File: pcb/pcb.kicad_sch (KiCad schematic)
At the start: 71 parts, among them J1 WH, J2 RGB, J3 220, Q1 AO3400A, Q2 AO3400A, Q3 AO3400A, Q4 AO3400A, Q5 AOD452, Q6 DTD114E, Q7 AO3400A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

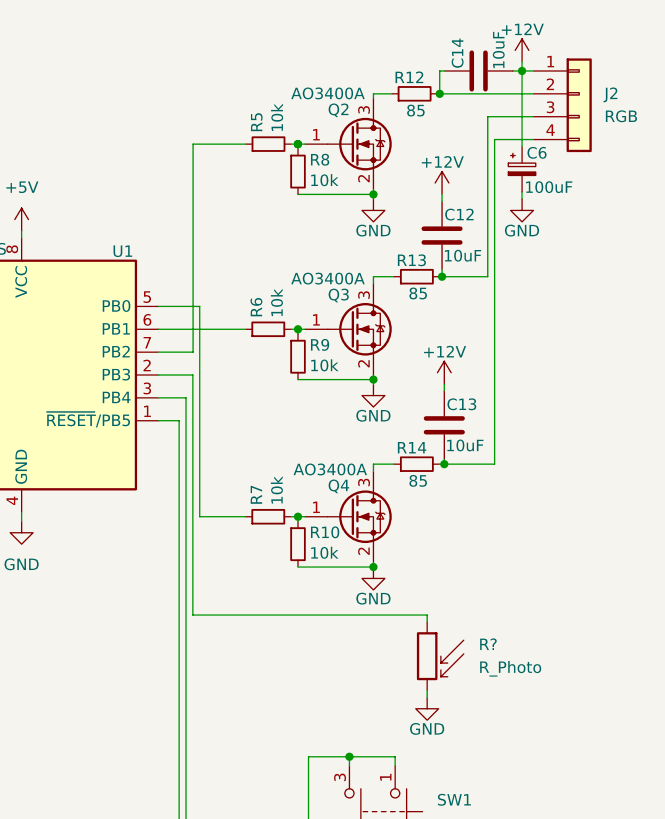
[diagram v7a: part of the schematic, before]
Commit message: light sensor added completely
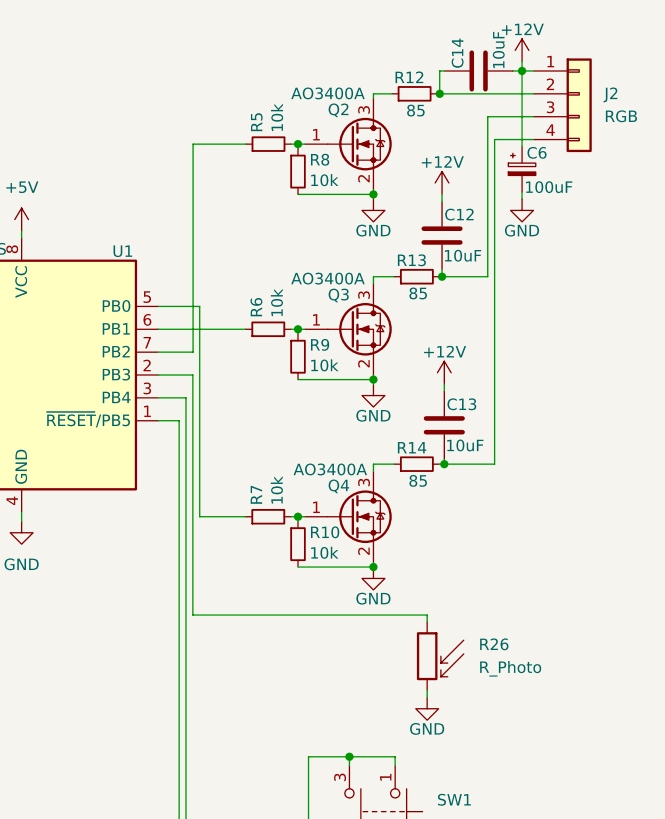
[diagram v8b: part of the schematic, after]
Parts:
- R26: renamed from R?; footprint (none) -> LED_THT:LED_D3.0mm
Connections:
- net at Q2.1 (G), R8.1: now also R5.2
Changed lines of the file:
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@@
   (junction (at 132.7404 45.974) (diameter 0) (color 0 0 0 0)
   )
+  (junction (at 230.759 27.432) (diameter 0) (color 0 0 0 0)
+  )
   (junction (at 76.3524 65.786) (diameter 0) (color 0 0 0 0)
   )
@@
   (junction (at 230.759 48.006) (diameter 0) (color 0 0 0 0)
   )
-  (junction (at 230.759 27.432) (diameter 0) (color 0 0 0 0)
-  )
   (junction (at 126.2634 65.786) (diameter 0) (color 0 0 0 0)
   )
@@
   (junction (at 173.8884 65.786) (diameter 0) (color 0 0 0 0)
   )
-  (junction (at 230.7336 27.432) (diameter 0) (color 0 0 0 0)
-  )
   (junction (at 118.7704 30.48) (diameter 0) (color 0 0 0 0)
   )
@@
     (stroke (width 0) (type default) (color 0 0 0 0))
   )
-  (wire (pts (xy 230.759 27.94) (xy 230.759 27.432))
-    (stroke (width 0) (type default) (color 0 0 0 0))
-  )
   (wire (pts (xy 132.7404 52.07) (xy 132.7404 53.848))
     (stroke (width 0) (type default) (color 0 0 0 0))
@@
     (stroke (width 0) (type default) (color 0 0 0 0))
   )
+  (wire (pts (xy 230.759 27.432) (xy 230.759 27.94))
+    (stroke (width 0) (type default) (color 0 0 0 0))
+  )
   (wire (pts (xy 247.015 62.992) (xy 252.603 62.992))
     (stroke (width 0) (type default) (color 0 0 0 0))
@@
     (stroke (width 0) (type default) (color 0 0 0 0))
   )
+  (wire (pts (xy 219.1004 27.432) (xy 224.9424 27.432))
+    (stroke (width 0) (type default) (color 0 0 0 0))
+  )
   (wire (pts (xy 99.4664 65.786) (xy 83.4644 65.786))
     (stroke (width 0) (type default) (color 0 0 0 0))
@@
     (stroke (width 0) (type default) (color 0 0 0 0))
   )
+  (wire (pts (xy 230.759 27.432) (xy 231.521 27.432))
+    (stroke (width 0) (type default) (color 0 0 0 0))
+  )
   (wire (pts (xy 117.7544 53.086) (xy 118.7704 53.086))
     (stroke (width 0) (type default) (color 0 0 0 0))
@@
     (stroke (width 0) (type default) (color 0 0 0 0))
   )
-  (wire (pts (xy 230.0224 27.432) (xy 230.7336 27.432))
-    (stroke (width 0) (type default) (color 0 0 0 0))
-  )
   (wire (pts (xy 153.5684 45.974) (xy 155.8544 45.974))
     (stroke (width 0) (type default) (color 0 0 0 0))
@@
     (stroke (width 0) (type default) (color 0 0 0 0))
   )
-  (wire (pts (xy 230.759 27.432) (xy 231.521 27.432))
-    (stroke (width 0) (type default) (color 0 0 0 0))
-  )
   (wire (pts (xy 117.7544 58.166) (xy 118.7704 58.166))
     (stroke (width 0) (type default) (color 0 0 0 0))
@@
     (stroke (width 0) (type default) (color 0 0 0 0))
   )
+  (wire (pts (xy 230.0224 27.432) (xy 230.759 27.432))
+    (stroke (width 0) (type default) (color 0 0 0 0))
+  )
   (wire (pts (xy 236.474 107.188) (xy 236.474 106.68))
     (stroke (width 0) (type default) (color 0 0 0 0))
@@
   )
   (wire (pts (xy 30.3784 58.42) (xy 30.3784 60.96))
-    (stroke (width 0) (type default) (color 0 0 0 0))
-  )
-  (wire (pts (xy 219.1004 27.432) (xy 224.9424 27.432))
     (stroke (width 0) (type default) (color 0 0 0 0))
   )
@@
   (symbol (lib_id "Device:R_Photo") (at 245.11 84.328 0) (mirror y) (unit 1)
     (in_bom yes) (on_board yes) (fields_autoplaced)
-    (property "Reference" "R?" (id 0) (at 250.825 83.0579 0)
+    (property "Reference" "R26" (id 0) (at 250.825 83.0579 0)
       (effects (font (size 1.27 1.27)) (justify right))
     )
@@
       (effects (font (size 1.27 1.27)) (justify right))
     )
-    (property "Footprint" "" (id 2) (at 243.84 90.678 90)
+    (property "Footprint" "LED_THT:LED_D3.0mm" (id 2) (at 243.84 90.678 90)
       (effects (font (size 1.27 1.27)) (justify left) hide)
     )
@@
   (symbol (lib_id "power:GND") (at 245.11 88.9 0) (unit 1)
     (in_bom yes) (on_board yes)
-    (property "Reference" "#PWR?" (id 0) (at 245.11 95.25 0)
+    (property "Reference" "#PWR0106" (id 0) (at 245.11 95.25 0)
       (effects (font (size 1.27 1.27)) hide)
     )
@@
     )
     (path "/968d7a56-aa2d-48fe-86bb-0e482d1025fc"
-      (reference "#PWR?") (unit 1) (value "GND") (footprint "")
+      (reference "#PWR0106") (unit 1) (value "GND") (footprint "")
     )
     (path "/89dde5cc-137e-4ed6-914c-22ceee3018f9"
@@
     )
     (path "/8c334f51-6a0b-406c-9f2c-47b0eaeba7c1"
-      (reference "R?") (unit 1) (value "R_Photo") (footprint "")
+      (reference "R26") (unit 1) (value "R_Photo") (footprint "LED_THT:LED_D3.0mm")
     )
     (path "/2538c6cb-070d-4b13-90b4-b662a536c3cb"
